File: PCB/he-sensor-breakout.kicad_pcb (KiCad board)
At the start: 2 copper layers, 19.1 x 29.1 mm, 13 parts, among them J1 Conn_01x03, U1 SLSS49E

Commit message: makes sensor matrix
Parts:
- added C1: 100n, Capacitor_SMD:C_0603_1608Metric, B.Cu at (78.0, 69.4)
- added C1: 100n, Capacitor_SMD:C_0603_1608Metric, B.Cu at (116.2, 69.5)
- added C1: 100n, Capacitor_SMD:C_0603_1608Metric, B.Cu at (97.1, 98.3)
- added C1: 100n, Capacitor_SMD:C_0603_1608Metric, B.Cu at (154.4, 98.6)
- added C1: 100n, Capacitor_SMD:C_0603_1608Metric, B.Cu at (116.2, 98.6)
- added C1: 100n, Capacitor_SMD:C_0603_1608Metric, B.Cu at (135.3, 98.6)
- added C1: 100n, Capacitor_SMD:C_0603_1608Metric, B.Cu at (135.3, 69.5)
- added C1: 100n, Capacitor_SMD:C_0603_1608Metric, B.Cu at (100.0, 70.2)
- added C1: 100n, Capacitor_SMD:C_0603_1608Metric, B.Cu at (154.4, 69.5)
- added H1: MountingHole_2.2mm_M2, MountingHole:MountingHole_2.2mm_M2, F.Cu at (93.9, 84.8)
- added H1: MountingHole_2.2mm_M2, MountingHole:MountingHole_2.2mm_M2, F.Cu at (113.1, 55.8)
- added H1: MountingHole_2.2mm_M2, MountingHole:MountingHole_2.2mm_M2, F.Cu at (74.8, 55.8)
- added H1: MountingHole_2.2mm_M2, MountingHole:MountingHole_2.2mm_M2, F.Cu at (94.0, 55.8)
- added H1: MountingHole_2.2mm_M2, MountingHole:MountingHole_2.2mm_M2, F.Cu at (132.2, 55.8)
- added H1: MountingHole_2.2mm_M2, MountingHole:MountingHole_2.2mm_M2, F.Cu at (132.0, 84.8)
- added H1: MountingHole_2.2mm_M2, MountingHole:MountingHole_2.2mm_M2, F.Cu at (112.9, 84.8)
- added H1: MountingHole_2.2mm_M2, MountingHole:MountingHole_2.2mm_M2, F.Cu at (151.2, 84.9)
- added H1: MountingHole_2.2mm_M2, MountingHole:MountingHole_2.2mm_M2, F.Cu at (151.3, 55.8)
- added H2: MountingHole_2.2mm_M2, MountingHole:MountingHole_2.2mm_M2, F.Cu at (125.2, 55.8)
- added H2: MountingHole_2.2mm_M2, MountingHole:MountingHole_2.2mm_M2, F.Cu at (87.0, 55.8)
- added H2: MountingHole_2.2mm_M2, MountingHole:MountingHole_2.2mm_M2, F.Cu at (106.1, 84.8)
- added H2: MountingHole_2.2mm_M2, MountingHole:MountingHole_2.2mm_M2, F.Cu at (144.4, 55.8)
- added H2: MountingHole_2.2mm_M2, MountingHole:MountingHole_2.2mm_M2, F.Cu at (163.5, 55.8)
- added H2: MountingHole_2.2mm_M2, MountingHole:MountingHole_2.2mm_M2, F.Cu at (163.4, 84.9)
- added H2: MountingHole_2.2mm_M2, MountingHole:MountingHole_2.2mm_M2, F.Cu at (125.1, 84.8)
- added H2: MountingHole_2.2mm_M2, MountingHole:MountingHole_2.2mm_M2, F.Cu at (106.2, 55.8)
- added H2: MountingHole_2.2mm_M2, MountingHole:MountingHole_2.2mm_M2, F.Cu at (144.2, 84.8)
- added H3: MountingHole_2.2mm_M2, MountingHole:MountingHole_2.2mm_M2, F.Cu at (151.3, 78.1)
- added H3: MountingHole_2.2mm_M2, MountingHole:MountingHole_2.2mm_M2, F.Cu at (151.2, 107.2)
- added H3: MountingHole_2.2mm_M2, MountingHole:MountingHole_2.2mm_M2, F.Cu at (132.2, 78.1)
- added H3: MountingHole_2.2mm_M2, MountingHole:MountingHole_2.2mm_M2, F.Cu at (132.0, 107.2)
- added H3: MountingHole_2.2mm_M2, MountingHole:MountingHole_2.2mm_M2, F.Cu at (113.1, 78.1)
- added H3: MountingHole_2.2mm_M2, MountingHole:MountingHole_2.2mm_M2, F.Cu at (94.0, 78.1)
- added H3: MountingHole_2.2mm_M2, MountingHole:MountingHole_2.2mm_M2, F.Cu at (112.9, 107.2)
- added H3: MountingHole_2.2mm_M2, MountingHole:MountingHole_2.2mm_M2, F.Cu at (93.9, 107.2)
- added H3: MountingHole_2.2mm_M2, MountingHole:MountingHole_2.2mm_M2, F.Cu at (74.8, 78.1)
- added H4: MountingHole_2.2mm_M2, MountingHole:MountingHole_2.2mm_M2, F.Cu at (87.0, 78.1)
- added H4: MountingHole_2.2mm_M2, MountingHole:MountingHole_2.2mm_M2, F.Cu at (106.2, 78.1)
- added H4: MountingHole_2.2mm_M2, MountingHole:MountingHole_2.2mm_M2, F.Cu at (125.1, 107.2)
- added H4: MountingHole_2.2mm_M2, MountingHole:MountingHole_2.2mm_M2, F.Cu at (106.1, 107.2)
- added H4: MountingHole_2.2mm_M2, MountingHole:MountingHole_2.2mm_M2, F.Cu at (144.4, 78.1)
- added H4: MountingHole_2.2mm_M2, MountingHole:MountingHole_2.2mm_M2, F.Cu at (163.4, 107.2)
- added H4: MountingHole_2.2mm_M2, MountingHole:MountingHole_2.2mm_M2, F.Cu at (125.2, 78.1)
- added H4: MountingHole_2.2mm_M2, MountingHole:MountingHole_2.2mm_M2, F.Cu at (144.2, 107.2)
- added H4: MountingHole_2.2mm_M2, MountingHole:MountingHole_2.2mm_M2, F.Cu at (163.5, 78.1)
- added J1: Conn_01x03, Connector_PinHeader_2.54mm:PinHeader_1x03_P2.54mm_Vertical, B.Cu at (102.5, 88.4)
- added J1: Conn_01x03, Connector_PinHeader_2.54mm:PinHeader_1x03_P2.54mm_Vertical, B.Cu at (121.6, 88.4)
- added J1: Conn_01x03, Connector_PinHeader_2.54mm:PinHeader_1x03_P2.54mm_Vertical, B.Cu at (140.8, 59.3)
- added J1: Conn_01x03, Connector_PinHeader_2.54mm:PinHeader_1x03_P2.54mm_Vertical, B.Cu at (159.8, 88.4)
- added J1: Conn_01x03, Connector_PinHeader_2.54mm:PinHeader_1x03_P2.54mm_Vertical, B.Cu at (102.6, 59.3)
- added J1: Conn_01x03, Connector_PinHeader_2.54mm:PinHeader_1x03_P2.54mm_Vertical, B.Cu at (121.7, 59.3)
- added J1: Conn_01x03, Connector_PinHeader_2.54mm:PinHeader_1x03_P2.54mm_Vertical, B.Cu at (83.5, 59.3)
- added J1: Conn_01x03, Connector_PinHeader_2.54mm:PinHeader_1x03_P2.54mm_Vertical, B.Cu at (140.7, 88.4)
- added J1: Conn_01x03, Connector_PinHeader_2.54mm:PinHeader_1x03_P2.54mm_Vertical, B.Cu at (160.0, 59.3)
- added MOUSE1: mouse-bite-19mm, Panelization:mouse-bite-19mm, F.Cu at (100.0, 86.5)
- added MOUSE1: mouse-bite-19mm, Panelization:mouse-bite-19mm, F.Cu at (119.0, 86.5)
- added MOUSE1: mouse-bite-19mm, Panelization:mouse-bite-19mm, F.Cu at (119.1, 57.4)
- added MOUSE1: mouse-bite-19mm, Panelization:mouse-bite-19mm, F.Cu at (138.3, 57.4)
- added MOUSE1: mouse-bite-19mm, Panelization:mouse-bite-19mm, F.Cu at (100.1, 57.4)
- added MOUSE1: mouse-bite-19mm, Panelization:mouse-bite-19mm, F.Cu at (157.2, 86.5)
- added MOUSE1: mouse-bite-19mm, Panelization:mouse-bite-19mm, F.Cu at (157.4, 57.4)
- added MOUSE1: mouse-bite-19mm, Panelization:mouse-bite-19mm, F.Cu at (80.9, 57.4)
- added MOUSE1: mouse-bite-19mm, Panelization:mouse-bite-19mm, F.Cu at (138.1, 86.5)
- added MOUSE2: mouse-bite-19mm, Panelization:mouse-bite-19mm, F.Cu at (138.3, 76.5)
- added MOUSE2: mouse-bite-19mm, Panelization:mouse-bite-19mm, F.Cu at (80.9, 76.5)
- added MOUSE2: mouse-bite-19mm, Panelization:mouse-bite-19mm, F.Cu at (119.2, 76.5)
- added MOUSE2: mouse-bite-19mm, Panelization:mouse-bite-19mm, F.Cu at (157.4, 76.5)
- added MOUSE2: mouse-bite-19mm, Panelization:mouse-bite-19mm, F.Cu at (100.1, 76.5)
- added MOUSE2: mouse-bite-19mm, Panelization:mouse-bite-19mm, F.Cu at (100.0, 105.5)
- added MOUSE2: mouse-bite-19mm, Panelization:mouse-bite-19mm, F.Cu at (138.1, 105.5)
- added MOUSE2: mouse-bite-19mm, Panelization:mouse-bite-19mm, F.Cu at (119.0, 105.5)
- added MOUSE2: mouse-bite-19mm, Panelization:mouse-bite-19mm, F.Cu at (157.3, 105.6)
- added REF**: SOT-23-5, Package_TO_SOT_SMD:SOT-23-5, B.Cu at (119.1, 63.8)
- added REF**: SOT-23-5, Package_TO_SOT_SMD:SOT-23-5, B.Cu at (157.3, 63.7)
- added REF**: SOT-23-5, Package_TO_SOT_SMD:SOT-23-5, B.Cu at (138.2, 63.8)
- added STB1: PinHeader_1x01_P2.54mm_Vertical, Connector_PinHeader_2.54mm:PinHeader_1x01_P2.54mm_Vertical, B.Cu at (130.7, 59.3)
- added STB1: PinHeader_1x01_P2.54mm_Vertical, Connector_PinHeader_2.54mm:PinHeader_1x01_P2.54mm_Vertical, B.Cu at (111.5, 59.3)
- added STB1: PinHeader_1x01_P2.54mm_Vertical, Connector_PinHeader_2.54mm:PinHeader_1x01_P2.54mm_Vertical, B.Cu at (149.8, 59.3)
- added STB1: PinHeader_1x01_P2.54mm_Vertical, Connector_PinHeader_2.54mm:PinHeader_1x01_P2.54mm_Vertical, B.Cu at (92.4, 88.4)
- added STB1: PinHeader_1x01_P2.54mm_Vertical, Connector_PinHeader_2.54mm:PinHeader_1x01_P2.54mm_Vertical, B.Cu at (111.4, 88.4)
- added STB1: PinHeader_1x01_P2.54mm_Vertical, Connector_PinHeader_2.54mm:PinHeader_1x01_P2.54mm_Vertical, B.Cu at (92.5, 59.3)
- added STB1: PinHeader_1x01_P2.54mm_Vertical, Connector_PinHeader_2.54mm:PinHeader_1x01_P2.54mm_Vertical, B.Cu at (130.5, 88.4)
- added STB1: PinHeader_1x01_P2.54mm_Vertical, Connector_PinHeader_2.54mm:PinHeader_1x01_P2.54mm_Vertical, B.Cu at (73.3, 59.3)
- added STB1: PinHeader_1x01_P2.54mm_Vertical, Connector_PinHeader_2.54mm:PinHeader_1x01_P2.54mm_Vertical, B.Cu at (149.7, 88.4)
- added STB2: PinHeader_1x01_P2.54mm_Vertical, Connector_PinHeader_2.54mm:PinHeader_1x01_P2.54mm_Vertical, B.Cu at (126.7, 88.4)
- added STB2: PinHeader_1x01_P2.54mm_Vertical, Connector_PinHeader_2.54mm:PinHeader_1x01_P2.54mm_Vertical, B.Cu at (88.5, 59.3)
- added STB2: PinHeader_1x01_P2.54mm_Vertical, Connector_PinHeader_2.54mm:PinHeader_1x01_P2.54mm_Vertical, B.Cu at (107.7, 59.3)
- added STB2: PinHeader_1x01_P2.54mm_Vertical, Connector_PinHeader_2.54mm:PinHeader_1x01_P2.54mm_Vertical, B.Cu at (165.0, 59.3)
- added STB2: PinHeader_1x01_P2.54mm_Vertical, Connector_PinHeader_2.54mm:PinHeader_1x01_P2.54mm_Vertical, B.Cu at (107.6, 88.4)
- added STB2: PinHeader_1x01_P2.54mm_Vertical, Connector_PinHeader_2.54mm:PinHeader_1x01_P2.54mm_Vertical, B.Cu at (164.9, 88.4)
- added STB2: PinHeader_1x01_P2.54mm_Vertical, Connector_PinHeader_2.54mm:PinHeader_1x01_P2.54mm_Vertical, B.Cu at (145.9, 59.3)
- added STB2: PinHeader_1x01_P2.54mm_Vertical, Connector_PinHeader_2.54mm:PinHeader_1x01_P2.54mm_Vertical, B.Cu at (145.7, 88.4)
- added STB2: PinHeader_1x01_P2.54mm_Vertical, Connector_PinHeader_2.54mm:PinHeader_1x01_P2.54mm_Vertical, B.Cu at (126.8, 59.3)
- added STB3: PinHeader_1x03_P2.54mm_Vertical, Connector_PinHeader_2.54mm:PinHeader_1x03_P2.54mm_Vertical, B.Cu at (83.5, 74.6)
- added STB3: PinHeader_1x03_P2.54mm_Vertical, Connector_PinHeader_2.54mm:PinHeader_1x03_P2.54mm_Vertical, B.Cu at (121.6, 103.6)
- added STB3: PinHeader_1x03_P2.54mm_Vertical, Connector_PinHeader_2.54mm:PinHeader_1x03_P2.54mm_Vertical, B.Cu at (159.8, 103.6)
- added STB3: PinHeader_1x03_P2.54mm_Vertical, Connector_PinHeader_2.54mm:PinHeader_1x03_P2.54mm_Vertical, B.Cu at (160.0, 74.6)
- added STB3: PinHeader_1x03_P2.54mm_Vertical, Connector_PinHeader_2.54mm:PinHeader_1x03_P2.54mm_Vertical, B.Cu at (102.5, 103.6)
- added STB3: PinHeader_1x03_P2.54mm_Vertical, Connector_PinHeader_2.54mm:PinHeader_1x03_P2.54mm_Vertical, B.Cu at (140.8, 74.6)
- added STB3: PinHeader_1x03_P2.54mm_Vertical, Connector_PinHeader_2.54mm:PinHeader_1x03_P2.54mm_Vertical, B.Cu at (102.6, 74.6)
- added STB3: PinHeader_1x03_P2.54mm_Vertical, Connector_PinHeader_2.54mm:PinHeader_1x03_P2.54mm_Vertical, B.Cu at (140.7, 103.6)
- added STB3: PinHeader_1x03_P2.54mm_Vertical, Connector_PinHeader_2.54mm:PinHeader_1x03_P2.54mm_Vertical, B.Cu at (121.7, 74.6)
- added SW: SW_Lekker_MX_1.00u_PCB, Button_Switch_Keyboard:SW_Lekker_MX_1.00u_PCB, F.Cu at (80.9, 67.7)
- added SW: SW_Lekker_MX_1.00u_PCB, Button_Switch_Keyboard:SW_Lekker_MX_1.00u_PCB, F.Cu at (119.0, 96.8)
- added SW: SW_Lekker_MX_1.00u_PCB, Button_Switch_Keyboard:SW_Lekker_MX_1.00u_PCB, F.Cu at (138.3, 67.8)
- added SW: SW_Lekker_MX_1.00u_PCB, Button_Switch_Keyboard:SW_Lekker_MX_1.00u_PCB, F.Cu at (138.1, 96.8)
- added SW: SW_Lekker_MX_1.00u_PCB, Button_Switch_Keyboard:SW_Lekker_MX_1.00u_PCB, F.Cu at (119.2, 67.7)
- added SW: SW_Lekker_MX_1.00u_PCB, Button_Switch_Keyboard:SW_Lekker_MX_1.00u_PCB, F.Cu at (100.1, 67.7)
- added SW: SW_Lekker_MX_1.00u_PCB, Button_Switch_Keyboard:SW_Lekker_MX_1.00u_PCB, F.Cu at (157.4, 67.8)
- added SW: SW_Lekker_MX_1.00u_PCB, Button_Switch_Keyboard:SW_Lekker_MX_1.00u_PCB, F.Cu at (157.3, 96.8)
- added SW: SW_Lekker_MX_1.00u_PCB, Button_Switch_Keyboard:SW_Lekker_MX_1.00u_PCB, F.Cu at (100.0, 96.8)
- added U1: SLSS49E, Package_TO_SOT_SMD:SOT-23-3, B.Cu at (119.2, 67.7)
- added U1: SLSS49E, Package_TO_SOT_SMD:SOT-23-3, B.Cu at (138.1, 96.8)
- added U1: SLSS49E, Package_TO_SOT_SMD:SOT-23-3, B.Cu at (80.9, 67.7)
- added U1: SLSS49E, Package_TO_SOT_SMD:SOT-23-3, B.Cu at (138.3, 67.8)
- added U1: SLSS49E, Package_TO_SOT_SMD:SOT-23-3, B.Cu at (157.3, 96.8)
- added U1: SLSS49E, Package_TO_SOT_SMD:SOT-23-3, B.Cu at (119.0, 96.8)
- added U1: SLSS49E, Package_TO_SOT_SMD:SOT-23-3, B.Cu at (100.1, 67.7)
- added U1: SLSS49E, Package_TO_SOT_SMD:SOT-23-3, B.Cu at (100.0, 96.8)
- added U1: SLSS49E, Package_TO_SOT_SMD:SOT-23-3, B.Cu at (157.4, 67.8)
- C1: footprint Capacitor_SMD:C_0402_1005Metric -> Capacitor_SMD:C_0603_1608Metric
- moved C1 19.8 mm to (78.0, 98.5)
- moved MOUSE2 19.5 mm to (80.9, 105.5)
- moved STB3 19.5 mm to (83.5, 103.6)
- moved H2 19.5 mm to (87.0, 84.8)
- moved H4 19.5 mm to (87.0, 107.2)
- moved J1 19.5 mm to (83.5, 88.4)
- moved STB2 19.5 mm to (88.5, 88.4)
- moved SW 19.5 mm to (80.9, 96.8)
- moved U1 19.5 mm to (80.9, 96.8)
- moved H1 19.5 mm to (74.8, 84.8)
- moved H3 19.5 mm to (74.8, 107.2)
- moved MOUSE1 19.5 mm to (80.9, 86.5)
- moved STB1 19.5 mm to (73.3, 88.4)
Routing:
- net VCC: track 10.8 -> 125.2 mm
- net /Vout: track 7.96 -> 77.4 mm
- net GND: track 0.00 -> 22.1 mm, vias 0 -> 180
- net Sout: track 0.00 -> 9.23 mm
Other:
- board size 19.1 x 29.1 mm -> 95.3 x 57.9 mm

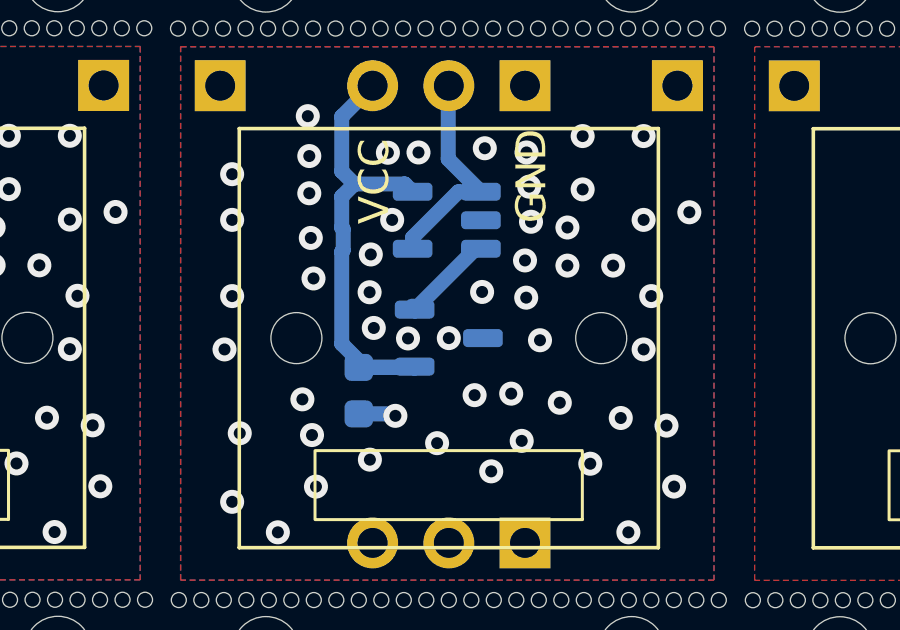
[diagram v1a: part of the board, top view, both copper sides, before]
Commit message: removes vias within hall sensor
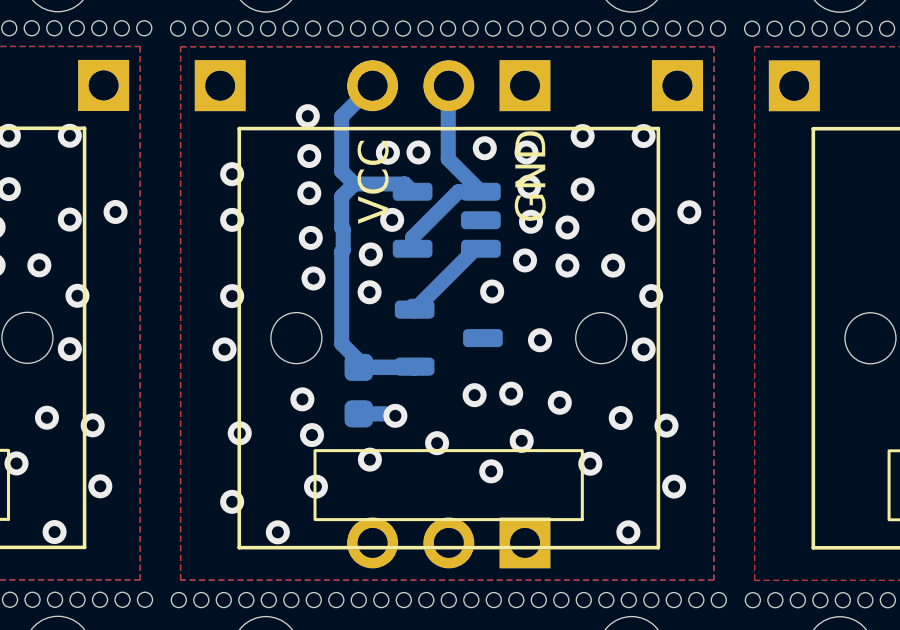
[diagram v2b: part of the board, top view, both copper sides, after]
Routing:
- net GND: vias 180 -> 176
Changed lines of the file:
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@@
   (via (at 82.0346 62.61125) (size 0.8) (drill 0.4) (layers "F.Cu" "B.Cu") (free) (net 2))
   (via (at 114.2736 69.784) (size 0.8) (drill 0.4) (layers "F.Cu" "B.Cu") (free) (net 2))
-  (via (at 140.8596 66.403451) (size 0.8) (drill 0.4) (layers "F.Cu" "B.Cu") (free) (net 2))
+  (via (at 139.725 66.2) (size 0.8) (drill 0.4) (layers "F.Cu" "B.Cu") (free) (net 2))
   (via (at 133.8516 72.701451) (size 0.8) (drill 0.4) (layers "F.Cu" "B.Cu") (free) (net 2))
   (via (at 141.3196 67.823451) (size 0.8) (drill 0.4) (layers "F.Cu" "B.Cu") (free) (net 2))
-  (via (at 138.28 67.752201) (size 0.8) (drill 0.4) (layers "F.Cu" "B.Cu") (free) (net 2))
   (via (at 122.2546 98.90125) (size 0.8) (drill 0.4) (layers "F.Cu" "B.Cu") (free) (net 2))
   (via (at 79.5846 64.54125) (size 0.8) (drill 0.4) (layers "F.Cu" "B.Cu") (free) (net 2))
@@
   (via (at 145.0276 66.351451) (size 0.8) (drill 0.4) (layers "F.Cu" "B.Cu") (free) (net 2))
   (via (at 82.0346 92.70125) (size 0.8) (drill 0.4) (layers "F.Cu" "B.Cu") (free) (net 2))
-  (via (at 139.3896 66.213451) (size 0.8) (drill 0.4) (layers "F.Cu" "B.Cu") (free) (net 2))
   (via (at 123.6156 62.786) (size 0.8) (drill 0.4) (layers "F.Cu" "B.Cu") (free) (net 2))
   (via (at 116.5136 66.214) (size 0.8) (drill 0.4) (layers "F.Cu" "B.Cu") (free) (net 2))
@@
   (via (at 122.075 65.075) (size 0.8) (drill 0.4) (layers "F.Cu" "B.Cu") (free) (net 2))
   (via (at 102.7796 96.77125) (size 0.8) (drill 0.4) (layers "F.Cu" "B.Cu") (free) (net 2))
-  (via (at 135.7796 67.413451) (size 0.8) (drill 0.4) (layers "F.Cu" "B.Cu") (free) (net 2))
   (via (at 125.6476 61.008) (size 0.8) (drill 0.4) (layers "F.Cu" "B.Cu") (free) (net 2))
   (via (at 144.7736 63.811451) (size 0.8) (drill 0.4) (layers "F.Cu" "B.Cu") (free) (net 2))
@@
   (via (at 144.2656 74.225451) (size 0.8) (drill 0.4) (layers "F.Cu" "B.Cu") (free) (net 2))
   (via (at 111.8646 95.78125) (size 0.8) (drill 0.4) (layers "F.Cu" "B.Cu") (free) (net 2))
-  (via (at 136.9196 67.763451) (size 0.8) (drill 0.4) (layers "F.Cu" "B.Cu") (free) (net 2))
   (via (at 112.9846 100.49125) (size 0.8) (drill 0.4) (layers "F.Cu" "B.Cu") (free) (net 2))
   (via (at 131.0576 63.811451) (size 0.8) (drill 0.4) (layers "F.Cu" "B.Cu") (free) (net 2))

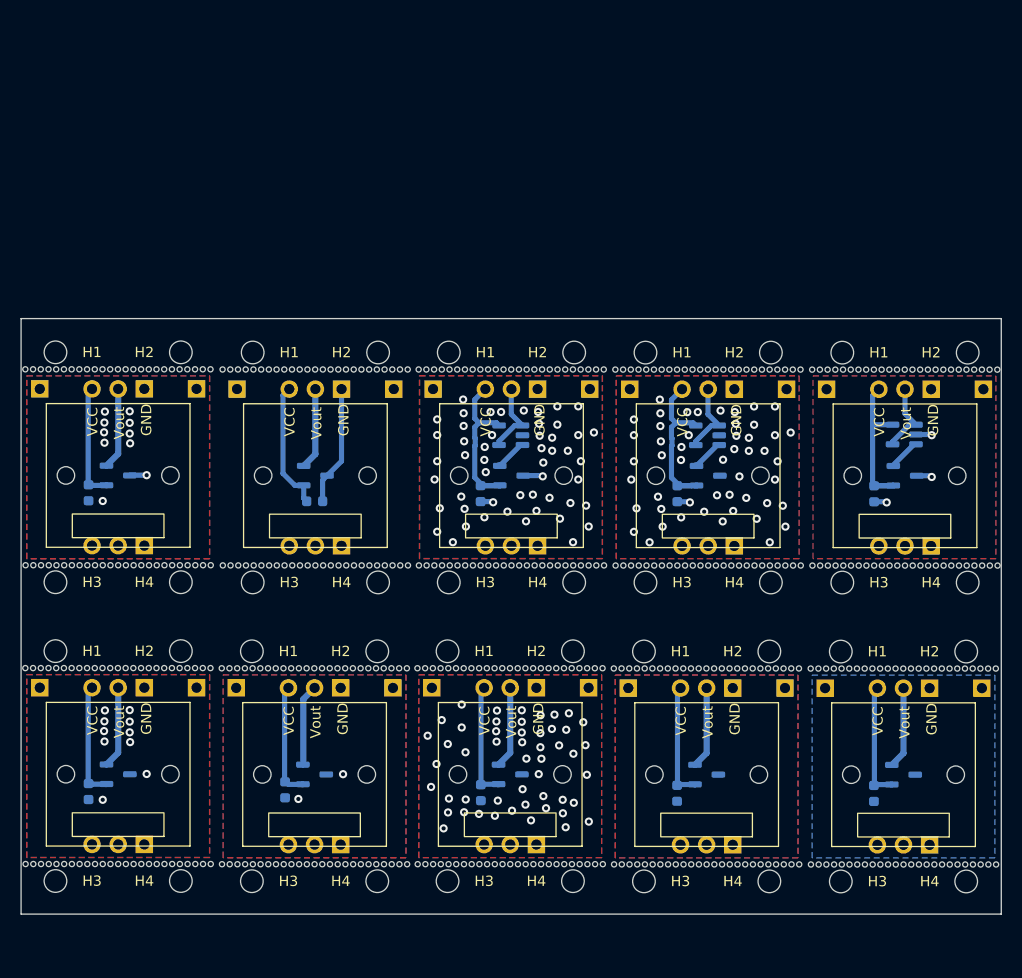
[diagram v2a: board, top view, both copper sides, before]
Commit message: adds another row to matrix
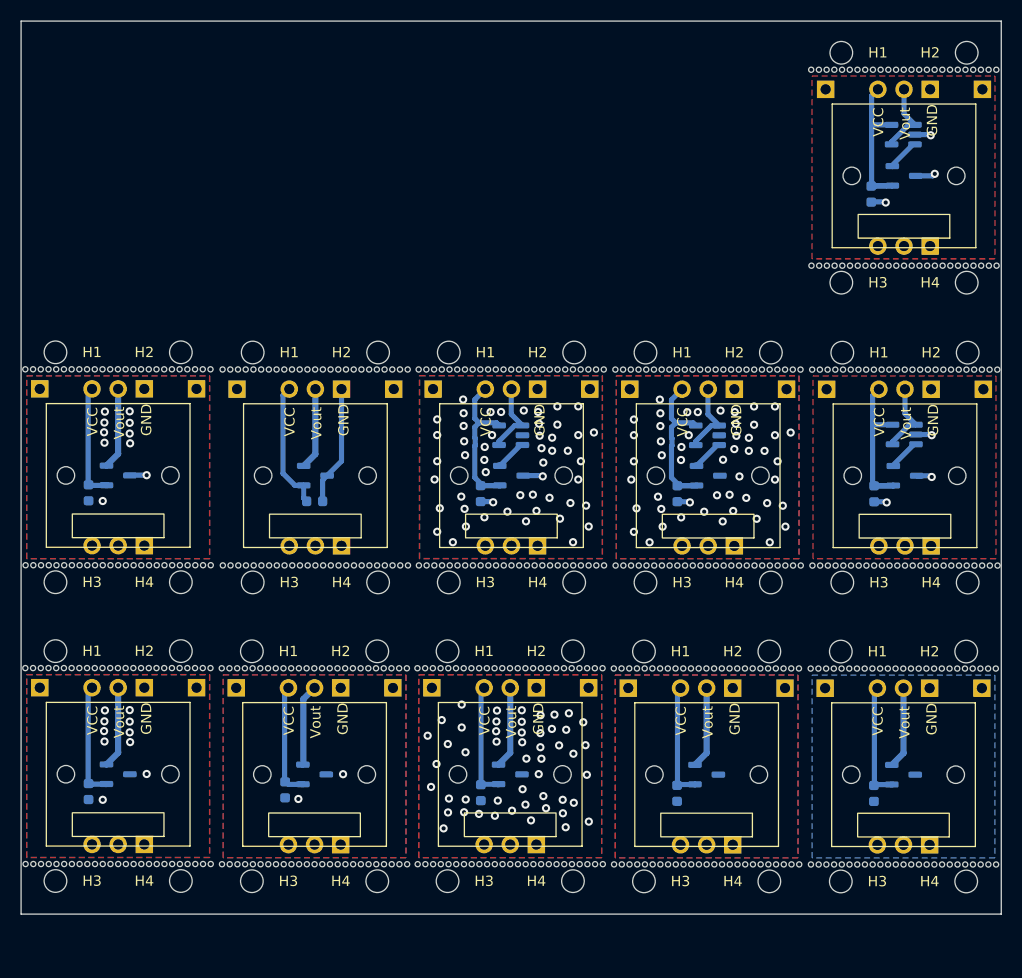
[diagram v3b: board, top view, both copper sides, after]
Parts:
- added C1: 100n, Capacitor_SMD:C_0603_1608Metric, B.Cu at (154.1, 40.4)
- added H1: MountingHole_2.2mm_M2, MountingHole:MountingHole_2.2mm_M2, F.Cu at (151.2, 26.6)
- added H2: MountingHole_2.2mm_M2, MountingHole:MountingHole_2.2mm_M2, F.Cu at (163.4, 26.6)
- added H3: MountingHole_2.2mm_M2, MountingHole:MountingHole_2.2mm_M2, F.Cu at (151.2, 49.0)
- added H4: MountingHole_2.2mm_M2, MountingHole:MountingHole_2.2mm_M2, F.Cu at (163.4, 49.0)
- added J1: Conn_01x03, Connector_PinHeader_2.54mm:PinHeader_1x03_P2.54mm_Vertical, B.Cu at (159.9, 30.2)
- added MOUSE1: mouse-bite-19mm, Panelization:mouse-bite-19mm, F.Cu at (157.3, 28.3)
- added MOUSE2: mouse-bite-19mm, Panelization:mouse-bite-19mm, F.Cu at (157.3, 47.3)
- added REF**: SOT-23-5, Package_TO_SOT_SMD:SOT-23-5, B.Cu at (157.2, 34.6)
- added STB1: PinHeader_1x01_P2.54mm_Vertical, Connector_PinHeader_2.54mm:PinHeader_1x01_P2.54mm_Vertical, B.Cu at (149.7, 30.2)
- added STB2: PinHeader_1x01_P2.54mm_Vertical, Connector_PinHeader_2.54mm:PinHeader_1x01_P2.54mm_Vertical, B.Cu at (164.9, 30.2)
- added STB3: PinHeader_1x03_P2.54mm_Vertical, Connector_PinHeader_2.54mm:PinHeader_1x03_P2.54mm_Vertical, B.Cu at (159.9, 45.4)
- added SW: SW_Lekker_MX_1.00u_PCB, Button_Switch_Keyboard:SW_Lekker_MX_1.00u_PCB, F.Cu at (157.3, 38.6)
- added U1: SLSS49E, Package_TO_SOT_SMD:SOT-23-3, B.Cu at (157.3, 38.6)
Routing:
- net VCC: track 125.2 -> 139.8 mm
- net /Vout: track 77.4 -> 84.5 mm
- net GND: track 22.1 -> 26.8 mm, vias 176 -> 179
- net Sout: track 9.23 -> 12.1 mm
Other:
- board size 95.3 x 57.9 mm -> 95.3 x 86.8 mm

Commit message: adds more test fixtures
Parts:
- added C1: 100n, Capacitor_SMD:C_0603_1608Metric, B.Cu at (154.5, 69.5)
- added H1: MountingHole_2.2mm_M2, MountingHole:MountingHole_2.2mm_M2, F.Cu at (151.2, 55.7)
- added H2: MountingHole_2.2mm_M2, MountingHole:MountingHole_2.2mm_M2, F.Cu at (163.4, 55.7)
- added H3: MountingHole_2.2mm_M2, MountingHole:MountingHole_2.2mm_M2, F.Cu at (151.2, 78.0)
- added H4: MountingHole_2.2mm_M2, MountingHole:MountingHole_2.2mm_M2, F.Cu at (163.4, 78.0)
- added J1: Conn_01x03, Connector_PinHeader_2.54mm:PinHeader_1x03_P2.54mm_Vertical, B.Cu at (159.9, 59.3)
- added MOUSE1: mouse-bite-19mm, Panelization:mouse-bite-19mm, F.Cu at (157.3, 57.3)
- added MOUSE2: mouse-bite-19mm, Panelization:mouse-bite-19mm, F.Cu at (157.3, 76.4)
- added STB1: PinHeader_1x01_P2.54mm_Vertical, Connector_PinHeader_2.54mm:PinHeader_1x01_P2.54mm_Vertical, B.Cu at (149.7, 59.3)
- added STB2: PinHeader_1x01_P2.54mm_Vertical, Connector_PinHeader_2.54mm:PinHeader_1x01_P2.54mm_Vertical, B.Cu at (164.9, 59.3)
- added STB3: PinHeader_1x03_P2.54mm_Vertical, Connector_PinHeader_2.54mm:PinHeader_1x03_P2.54mm_Vertical, B.Cu at (159.9, 74.5)
- added SW: SW_Lekker_MX_1.00u_PCB, Button_Switch_Keyboard:SW_Lekker_MX_1.00u_PCB, F.Cu at (157.3, 67.7)
- added U1: SLSS49E, Package_TO_SOT_SMD:SOT-23-3, B.Cu at (157.3, 67.7)
- moved H2 34.9 mm to (144.3, 26.6)
- moved H4 34.9 mm to (144.3, 49.0)
- moved REF** 34.9 mm to (138.1, 34.6)
- moved STB3 34.9 mm to (140.8, 45.4)
- moved C1 34.9 mm to (135.2, 40.3)
- moved J1 34.9 mm to (140.8, 30.2)
- moved MOUSE1 34.9 mm to (138.2, 28.3)
- moved STB2 34.9 mm to (145.8, 30.2)
- moved STB1 34.9 mm to (130.6, 30.2)
- moved H1 34.9 mm to (132.1, 26.6)
- moved H3 34.9 mm to (132.1, 49.0)
- moved MOUSE2 34.9 mm to (138.2, 47.3)
- moved SW 34.9 mm to (138.2, 38.6)
- moved U1 34.9 mm to (138.2, 38.6)
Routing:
- net VCC: track 139.8 -> 151.0 mm
- net /Vout: track 84.5 -> 92.4 mm
- net GND: track 26.8 -> 28.6 mm, vias 179 -> 180

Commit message: adds tb
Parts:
- removed H1 (x12), H2 (x12), H3 (x12), H4 (x12): MountingHole_2.2mm_M2, MountingHole:MountingHole_2.2mm_M2
- removed MOUSE1 (x12), MOUSE2 (x12): mouse-bite-19mm, Panelization:mouse-bite-19mm
- removed REF** (x3): SOT-23-5, Package_TO_SOT_SMD:SOT-23-5
- added C1: 100n, Capacitor_SMD:C_0603_1608Metric, B.Cu at (119.2, 59.2)
- added J1: Conn_01x03, Connector_PinHeader_2.54mm:PinHeader_1x03_P2.54mm_Vertical, B.Cu at (121.8, 48.3)
- added STB1: PinHeader_1x01_P2.54mm_Vertical, Connector_PinHeader_2.54mm:PinHeader_1x01_P2.54mm_Vertical, B.Cu at (111.7, 48.3)
- added STB2: PinHeader_1x01_P2.54mm_Vertical, Connector_PinHeader_2.54mm:PinHeader_1x01_P2.54mm_Vertical, B.Cu at (126.9, 48.3)
- added STB3: PinHeader_1x03_P2.54mm_Vertical, Connector_PinHeader_2.54mm:PinHeader_1x03_P2.54mm_Vertical, B.Cu at (121.8, 63.5)
- added SW: SW_Lekker_MX_1.00u_PCB, Button_Switch_Keyboard:SW_Lekker_MX_1.00u_PCB, F.Cu at (119.3, 56.7)
- added U1: SLSS49E, Package_TO_SOT_SMD:SOT-23-3, B.Cu at (119.3, 56.7)
- added U3: MCP6001, Package_TO_SOT_SMD:SOT-23-5, B.Cu at (138.3, 53.0)
- added U3: MCP6001, Package_TO_SOT_SMD:SOT-23-5, B.Cu at (119.2, 72.2)
- added U3: MCP6001, Package_TO_SOT_SMD:SOT-23-5, B.Cu at (138.3, 72.2)
- U3: renamed from REF**; value SOT-23-5 -> MCP6001
- moved STB2 18.5 mm to (164.9, 48.7)
- moved SW 18.4 mm to (138.4, 57.0)
- moved U1 18.4 mm to (138.4, 57.0)
- moved J1 18.4 mm to (141.0, 48.6)
- moved STB1 18.4 mm to (130.8, 48.6)
- moved STB2 18.4 mm to (146.0, 48.6)
- moved C1 18.4 mm to (154.3, 58.8)
- moved C1 18.4 mm to (135.4, 58.7)
- moved J1 18.4 mm to (160.1, 48.6)
- moved STB1 18.4 mm to (149.9, 48.6)
- moved STB3 18.4 mm to (141.0, 63.8)
- moved STB3 18.4 mm to (160.1, 63.8)
- moved SW 18.4 mm to (157.5, 57.0)
- moved U1 18.4 mm to (157.5, 57.0)
- moved U3 18.4 mm to (157.4, 53.0)
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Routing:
- net VCC: track 151.0 -> 163.6 mm
- net GND: track 28.6 -> 40.5 mm, vias 180 -> 178
- net /Vout: track 92.4 -> 100.4 mm
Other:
- board size 95.3 x 86.8 mm -> 95.3 x 60.3 mm
